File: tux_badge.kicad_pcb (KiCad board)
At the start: 2 copper layers, 44.9 x 52.1 mm, 5 parts, among them SW1 SW_Push

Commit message: routing finished
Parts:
- removed the REF** at (165.1, 75.9)
- added REF**: MountingHole_3.2mm_M3_DIN965, MountingHole:MountingHole_3.2mm_M3_DIN965, F.Cu at (165.1, 75.9)
- added REF**: KiCad-Logo2_5mm_SilkScreen, Symbol:KiCad-Logo2_5mm_SilkScreen, B.Cu at (152.2, 117.2)
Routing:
- net VCC: track 0.00 -> 56.6 mm, vias 0 -> 2
- net Net-(R1-Pad1): track 0.00 -> 42.0 mm
- net Net-(D1-Pad2): track 0.00 -> 2.16 mm
- net GND: vias 0 -> 6
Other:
- board text added: "Rev. 1.0"
- board text added: "Tux Badge"
- board text removed: "Tux Badge Rev. 1.0"

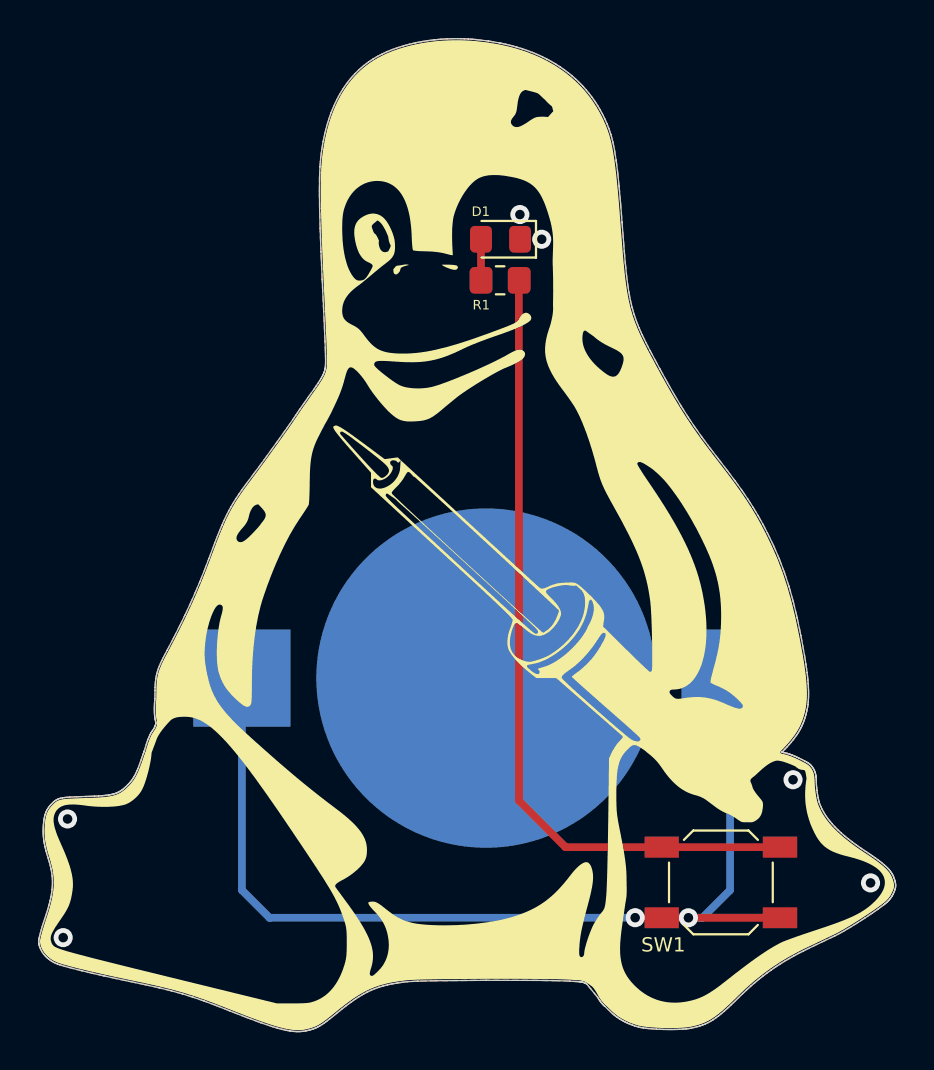
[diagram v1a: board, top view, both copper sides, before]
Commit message: changing position of resistor R1
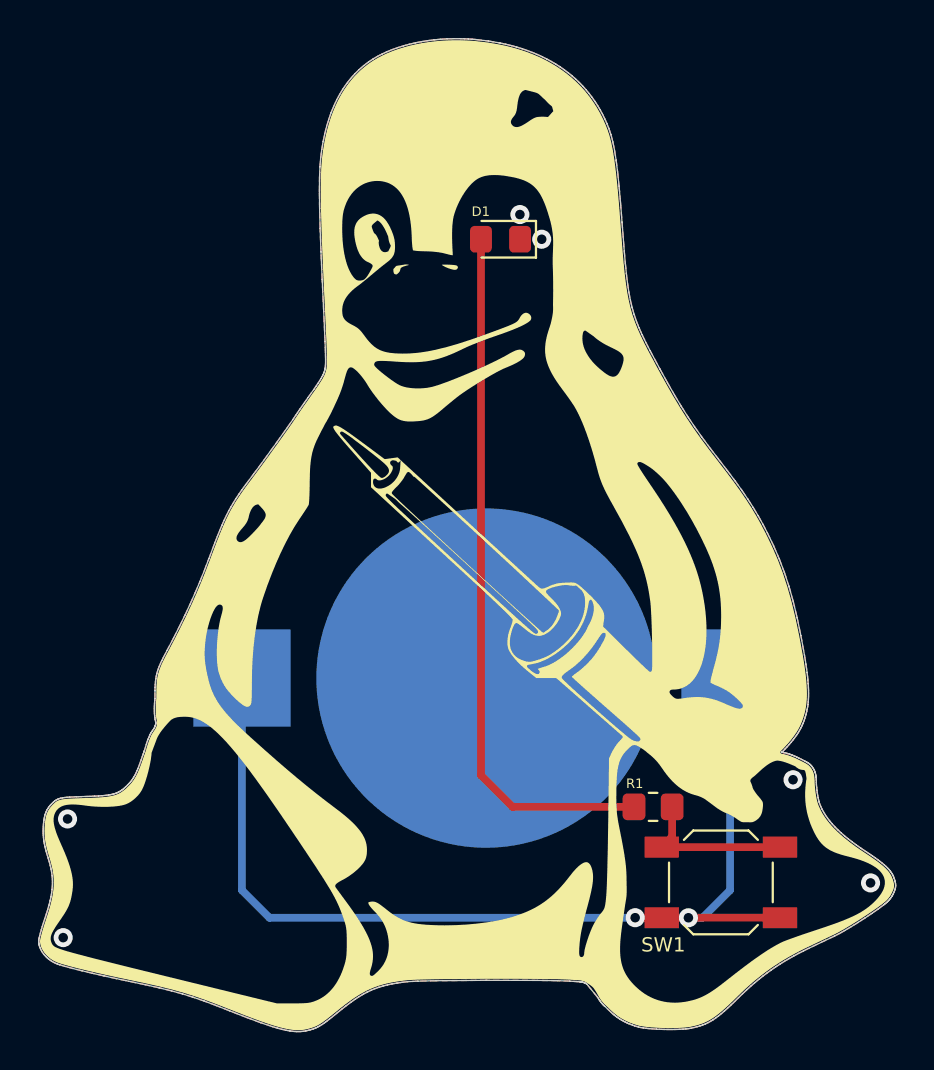
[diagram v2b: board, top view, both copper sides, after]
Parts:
- moved R1 28.8 mm to (175.4, 112.5)
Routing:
- net Net-(D1-Pad2): track 2.16 -> 36.8 mm
- net Net-(R1-Pad1): track 42.0 -> 8.54 mm
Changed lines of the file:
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@@
   )
   (footprint "Resistor_SMD:R_0805_2012Metric_Pad1.20x1.40mm_HandSolder" (layer "F.Cu")
-    (at 167.391014 84.856533 180)
+    (at 175.4124 112.4712 180)
     (descr "Resistor SMD 0805 (2012 Metric), square (rectangular) end terminal, IPC_7351 nominal with elongated pad for handsoldering. (Body size source: IPC-SM-782 page 72, https://www.pcb-3d.com/wordpress/wp-content/uploads/ipc-sm-782a_amendment_1_and_2.pdf), generated with kicad-footprint-generator")
     (tags "resistor handsolder")
@@
     (property "Sheetname" "")
     (attr smd exclude_from_pos_files exclude_from_bom)
-    (fp_text reference "R1" (at 0.9906 -1.2954) (layer "F.SilkS")
+    (fp_text reference "R1" (at 0.9652 1.2192) (layer "F.SilkS")
       (effects (font (size 0.5 0.5) (thickness 0.1)))
     )
@@
     (effects (font (size 1.75 1.75) (thickness 0.3)) (justify mirror))
   )
-  (segment (start 166.3864 84.851919) (end 166.391014 84.856533) (width 0.4064) (layer "F.Cu") (net 1))
-  (segment (start 166.3864 82.7024) (end 166.3864 84.851919) (width 0.4064) (layer "F.Cu") (net 1))
-  (segment (start 175.8684 114.5836) (end 170.8192 114.5836) (width 0.4064) (layer "F.Cu") (net 2))
-  (segment (start 170.8192 114.5836) (end 168.3766 112.141) (width 0.4064) (layer "F.Cu") (net 2))
-  (segment (start 168.3766 84.870947) (end 168.391014 84.856533) (width 0.4064) (layer "F.Cu") (net 2))
-  (segment (start 182.0684 114.5836) (end 175.8684 114.5836) (width 0.4064) (layer "F.Cu") (net 2))
-  (segment (start 168.3766 112.141) (end 168.3766 84.870947) (width 0.4064) (layer "F.Cu") (net 2))
+  (segment (start 174.4124 112.4712) (end 168.0464 112.4712) (width 0.4064) (layer "F.Cu") (net 1))
+  (segment (start 166.3864 110.8112) (end 166.3864 82.7024) (width 0.4064) (layer "F.Cu") (net 1))
+  (segment (start 168.0464 112.4712) (end 166.3864 110.8112) (width 0.4064) (layer "F.Cu") (net 1))
+  (segment (start 176.4124 112.4712) (end 176.4124 114.0396) (width 0.4064) (layer "F.Cu") (net 2))
+  (segment (start 175.8684 114.5836) (end 182.0684 114.5836) (width 0.4064) (layer "F.Cu") (net 2))
+  (segment (start 176.4124 114.0396) (end 175.8684 114.5836) (width 0.4064) (layer "F.Cu") (net 2))
   (segment (start 182.0684 118.2836) (end 175.8684 118.2836) (width 0.4064) (layer "F.Cu") (net 3))
   (segment (start 174.5276 118.2836) (end 175.8684 118.2836) (width 0.4064) (layer "F.Cu") (net 3))

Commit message: first order
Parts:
- removed REF**: MountingHole_3.2mm_M3_DIN965, MountingHole:MountingHole_3.2mm_M3_DIN965
- removed REF**: KiCad-Logo2_5mm_SilkScreen, Symbol:KiCad-Logo2_5mm_SilkScreen
- D1: value LED -> Yellow
- R1: value R -> 62
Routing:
- net GND: vias 6 -> 7
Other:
- board text added: "Tux-Badge"
- board text added: "https://www.lugsaar.de"
- board text removed: "Tux Badge"
- board text removed: "https://lugsaar.de"

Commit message: adding BOM and fixing losed silkscreen icons
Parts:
- added REF**: MountingHole_3.5mm, MountingHole:MountingHole_3.5mm, F.Cu at (165.2, 76.0)
- added REF**: KiCad-Logo2_5mm_SilkScreen, Symbol:KiCad-Logo2_5mm_SilkScreen, B.Cu at (151.9, 117.1)
